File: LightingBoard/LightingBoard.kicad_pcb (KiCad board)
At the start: 2 copper layers, 51.7 x 46.2 mm, 58 parts, among them J1 Barrel_Jack_Switch, J2 LED Out, J3 LED Out, J4 Programming, J5 UART, U1 AP7384-50SA, U2 NCV833, U3 INA180A2, U4 LMR33630ADDA, U5 MCP4725xxx-xCH, U6 INA180A2, U7 LMR33630ADDA, U8 MCP4725xxx-xCH, U9 ATtiny2313A-S

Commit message: NO MORR DINOSAURR
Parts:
- removed U1: AP7384-50SA, Package_TO_SOT_SMD:SOT-23
- added U10: AP2120N-5.0TRG1, Package_TO_SOT_SMD:SOT-23, F.Cu at (117.1, 86.9)
- U9: value ATtiny2313A-S -> ATtiny841-SS; footprint Package_SO:SOIC-20W_7.5x12.8mm_P1.27mm -> Package_SO:SOIC-14_3.9x8.7mm_P1.27mm
- moved J5 22.7 mm to (110.0, 76.7), turned to 0 degrees
- moved J1 17.9 mm to (115.8, 65.9), turned to -90 degrees
- moved C2 17.9 mm to (119.9, 91.7), turned to -90 degrees
- moved C5 16.5 mm to (120.1, 86.9), turned to -90 degrees
- moved U9 14.9 mm to (117.3, 78.0), turned to 180 degrees
- moved R11 13.0 mm to (119.4, 83.8), turned to 0 degrees
- moved C4 10.1 mm to (114.0, 86.9), turned to -90 degrees
- moved C18 9.53 mm to (115.6, 83.8), turned to 0 degrees
- moved D1 8.44 mm to (114.8, 70.9)
- moved R21 7.77 mm to (118.1, 70.9)
- moved R20 3.18 mm to (121.2, 70.9), turned to -90 degrees
- moved C3 1.85 mm to (112.0, 93.0), turned to -90 degrees
- moved C1 1.61 mm to (111.5, 70.9), turned to -90 degrees
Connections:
- C18 pad 1: /Reset -> GND
- C18 pad 2: GND -> /Reset
- J4 pad 2: Net-(J4-Pin_2) -> /SCL
- J4 pad 3: /SDA -> /MISO(12)
- J4 pad 4: Net-(J4-Pin_4) -> /MOSI(11)
- J4 pad 5: /SCL -> /CS(10)
- R11 pad 1: +5V -> /Reset
- R11 pad 2: /Reset -> +5V
- R2 pad 2: /SDA -> /MOSI(11)
- R20 pad 1: /Reset -> /CS(10)
- R20 pad 2: Net-(J4-Pin_2) -> /Reset
- U5 pad 4: /SDA -> /MOSI(11)
- U8 pad 4: /SDA -> /MOSI(11)
- U9 pad 1: /Reset -> +5V
- U9 pad 10: GND -> /Enable1
- U9 pad 11: unconnected-(U9-PD6-Pad11) -> /UART_RX
- U9 pad 12: /PG2 -> /UART_TX
- U9 pad 13: /Enable2 -> /PG1
- U9 pad 14: /PG1 -> GND
- U9 pad 2: /UART_RX -> /PG2
- U9 pad 3: /UART_TX -> /Enable2
- U9 pad 4: GND -> /Reset
- U9 pad 5: GND -> /Status
- U9 pad 7: unconnected-(U9-PD3-Pad7) -> /MOSI(11)
- U9 pad 8: unconnected-(U9-PD4-Pad8) -> /MISO(12)
- U9 pad 9: unconnected-(U9-PD5-Pad9) -> /SCL
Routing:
- net /SDA: track 40.7 -> 0.00 mm, vias 3 -> 0
- net /MOSI(11): track 0.00 -> 21.7 mm, vias 0 -> 1
- net Net-(J4-Pin_4): track 21.7 -> 0.00 mm, vias 2 -> 0
- net /PG1: track 16.5 -> 32.5 mm, vias 0 -> 2
- net /Enable1: track 5.08 -> 19.2 mm, vias 0 -> 2
- net /Enable2: track 27.7 -> 14.3 mm
- net /PG2: track 38.1 -> 24.8 mm
- net /MISO(12): track 0.00 -> 12.3 mm
- net /Reset: track 26.0 -> 15.8 mm, vias 4 -> 3
- net GND: track 0.00 -> 9.36 mm, vias 32 -> 31
- net /SCL: track 39.0 -> 29.7 mm, vias 4 -> 3
- net +5V: track 62.5 -> 54.5 mm, vias 4 -> 3
- net Net-(J4-Pin_2): track 6.88 -> 0.00 mm
- net VCC: track 109.0 -> 102.2 mm, vias 7 -> 8
- net /CS(10): track 0.00 -> 5.59 mm
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
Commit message: HEHEHE
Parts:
- added C19: 100nF, Capacitor_SMD:C_0603_1608Metric, F.Cu at (134.4, 68.8)
- added C20: 10uF, Capacitor_SMD:C_0603_1608Metric, F.Cu at (132.3, 72.9)
- added C21: 100nF, Capacitor_SMD:C_0603_1608Metric, F.Cu at (134.4, 80.5)
- added C22: 10uF, Capacitor_SMD:C_0603_1608Metric, F.Cu at (132.3, 76.7)
- added C23: 1u, Capacitor_SMD:C_0603_1608Metric, F.Cu at (144.3, 76.5)
- added C24: 100nF, Capacitor_SMD:C_0603_1608Metric, F.Cu at (144.3, 73.2)
- C12, C6: value .1u -> 100nF
- C2: value 47u -> 10u
- R14, R5: value 4k -> 30k
- R18, R9: value 1k -> 10k
- U2: value NCV833 -> TL5580IDR
- moved C6 3.84 mm to (149.4, 72.6), turned to 0 degrees
- moved C12 3.84 mm to (149.4, 76.7), turned to 0 degrees
- moved R2 0.51 mm to (129.5, 76.7)
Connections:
- net /SCL renamed /SCL(13)
- C12 pad 1: VCC -> +5V
- C6 pad 1: VCC -> +5V
- U3 pad 5: VCC -> +5V
- U6 pad 5: VCC -> +5V
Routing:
- net +5V: track 54.5 -> 93.6 mm, vias 3 -> 6
- net VCC: track 102.2 -> 90.5 mm, vias 8 -> 5
- net Net-(U2B-+): track 5.10 -> 5.91 mm, vias 0 -> 2
- net /VDAC2: track 5.62 -> 6.31 mm
- net /MOSI(11): track 21.7 -> 21.1 mm
- net /Sum2: track 34.6 -> 33.9 mm
- net Net-(U2B--): track 8.20 -> 8.83 mm, vias 0 -> 2
- net GND: vias 31 -> 35

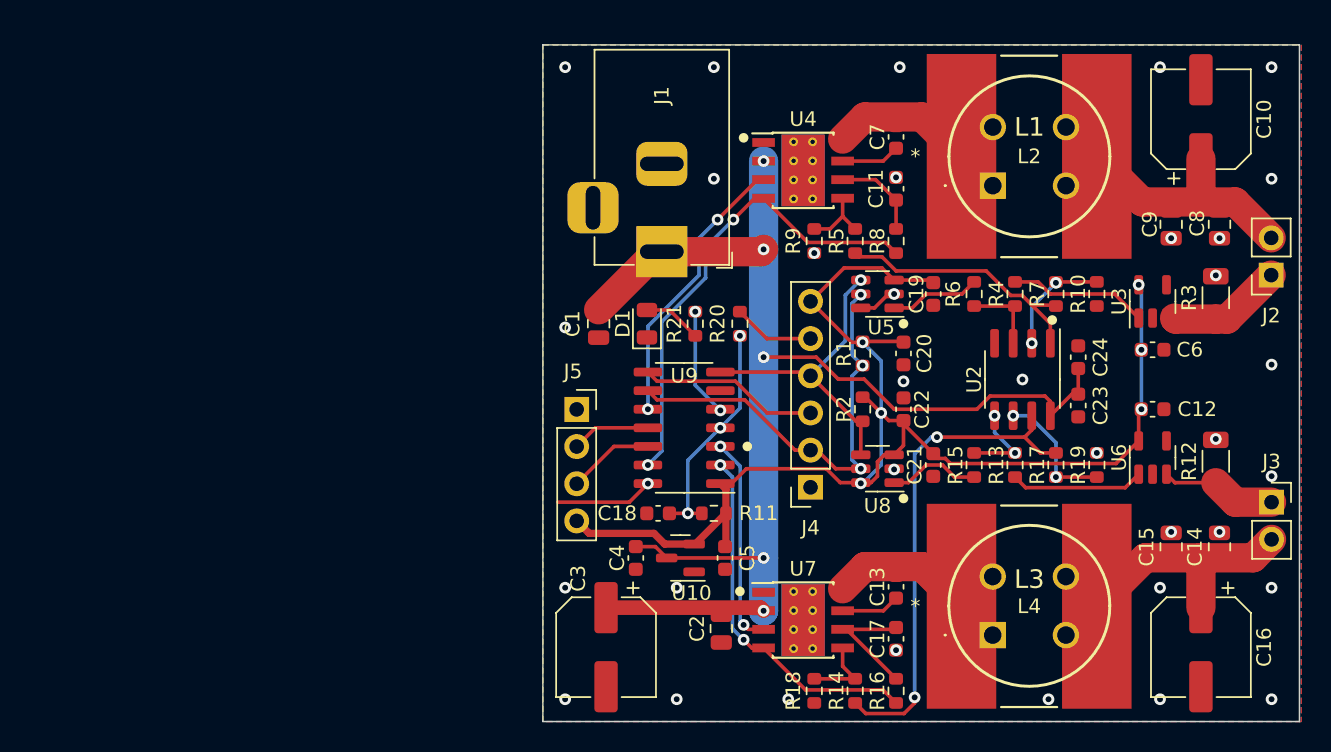
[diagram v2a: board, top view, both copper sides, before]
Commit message: new design based on AVR32DD20
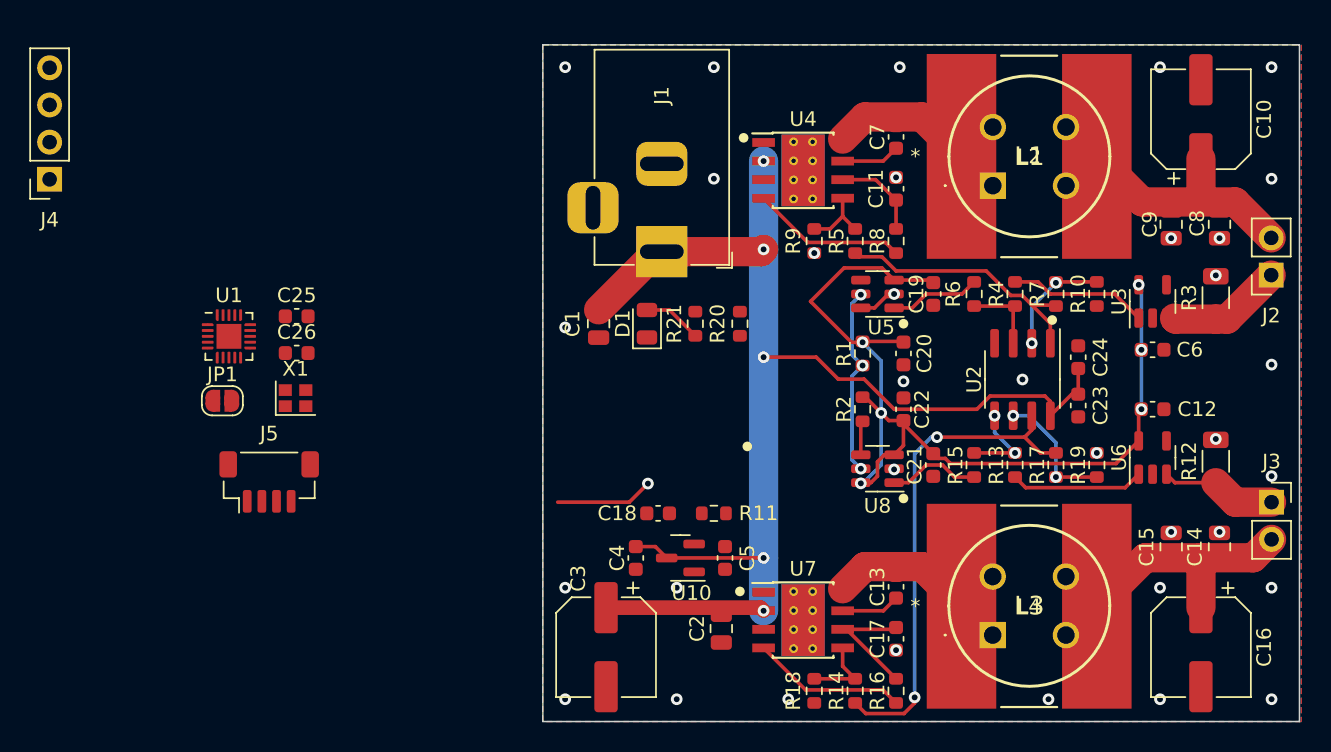
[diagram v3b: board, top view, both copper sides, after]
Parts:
- removed U9: ATtiny841-SS, Package_SO:SOIC-14_3.9x8.7mm_P1.27mm
- added C25: C_CLK, Capacitor_SMD:C_0603_1608Metric, F.Cu at (90.9, 70.4)
- added C26: C_CLK, Capacitor_SMD:C_0603_1608Metric, F.Cu at (90.9, 72.9)
- added JP1: SolderJumper_2_Open, Jumper:SolderJumper-2_P1.3mm_Open_RoundedPad1.0x1.5mm, F.Cu at (85.8, 76.1)
- added U1: AVR32DD20-E/REB, Package_DFN_QFN:VQFN-20-1EP_3x3mm_P0.4mm_EP1.7x1.7mm, F.Cu at (86.2, 71.7)
- added X1: XRCGB32M000F1S2KR0, Crystal:Crystal_SMD_2016-4Pin_2.0x1.6mm, F.Cu at (90.8, 76.0)
- J4: footprint Connector_PinSocket_2.54mm:PinSocket_1x06_P2.54mm_Vertical -> Connector_PinSocket_2.54mm:PinSocket_1x04_P2.54mm_Vertical
- J5: footprint Connector_PinSocket_2.54mm:PinSocket_1x04_P2.54mm_Vertical -> Connector_JST:JST_SH_BM04B-SRSS-TB_1x04-1MP_P1.00mm_Vertical
- L1, L3: footprint BuckParts:7447231101 -> CustomFootprints:7447231101
- L2, L4: footprint BuckParts:IND_BOURNS_SDR1307 -> CustomFootprints:IND_BOURNS_SDR1307
- R11: value 4.7k -> 330
- R20: value 330 -> 4.7K
- moved J4 56.1 mm to (74.0, 61.0)
- moved J5 21.6 mm to (89.0, 81.7)
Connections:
- C18 pad 2: /Reset -> Net-(U1-PF6(*RESET))
- J4 pad 2: /SCL(13) -> Net-(J4-Pin_2)
- J4 pad 3: /MISO(12) -> /Reset
- J4 pad 4: /MOSI(11) -> +5V
- J5 pad 2: /UART_RX -> +5V
- J5 pad 4: +5V -> /UART_RX
- R1 pad 2: /SCL(13) -> /SCL
- R11 pad 2: +5V -> Net-(U1-PF6(*RESET))
- R2 pad 2: /MOSI(11) -> /SDA
- R20 pad 1: /CS(10) -> /UPDI
- R20 pad 2: /Reset -> Net-(J4-Pin_2)
- U5 pad 4: /MOSI(11) -> /SDA
- U5 pad 5: /SCL(13) -> /SCL
- U8 pad 4: /MOSI(11) -> /SDA
- U8 pad 5: /SCL(13) -> /SCL
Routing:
- net /SCL(13): track 29.7 -> 0.00 mm, vias 3 -> 0
- net +5V: track 93.6 -> 66.7 mm
- net /PG1: track 32.5 -> 10.6 mm, vias 2 -> 0
- net /MOSI(11): track 21.1 -> 0.00 mm, vias 1 -> 0
- net /Enable1: track 19.2 -> 0.00 mm, vias 2 -> 0
- net /Reset: track 15.8 -> 0.00 mm, vias 3 -> 0
- net /Enable2: track 14.3 -> 0.00 mm, vias 2 -> 0
- net /PG2: track 24.8 -> 10.6 mm, vias 2 -> 0
- net /SCL: track 0.00 -> 13.0 mm, vias 0 -> 3
- net /MISO(12): track 12.3 -> 0.00 mm
- net /Status: track 7.46 -> 0.00 mm, vias 2 -> 0
- net /UART_TX: track 5.92 -> 0.00 mm
- net /CS(10): track 5.59 -> 0.00 mm
- net /UART_RX: track 5.40 -> 0.00 mm
- net /SDA: track 0.00 -> 1.97 mm

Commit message: update to kicad 8
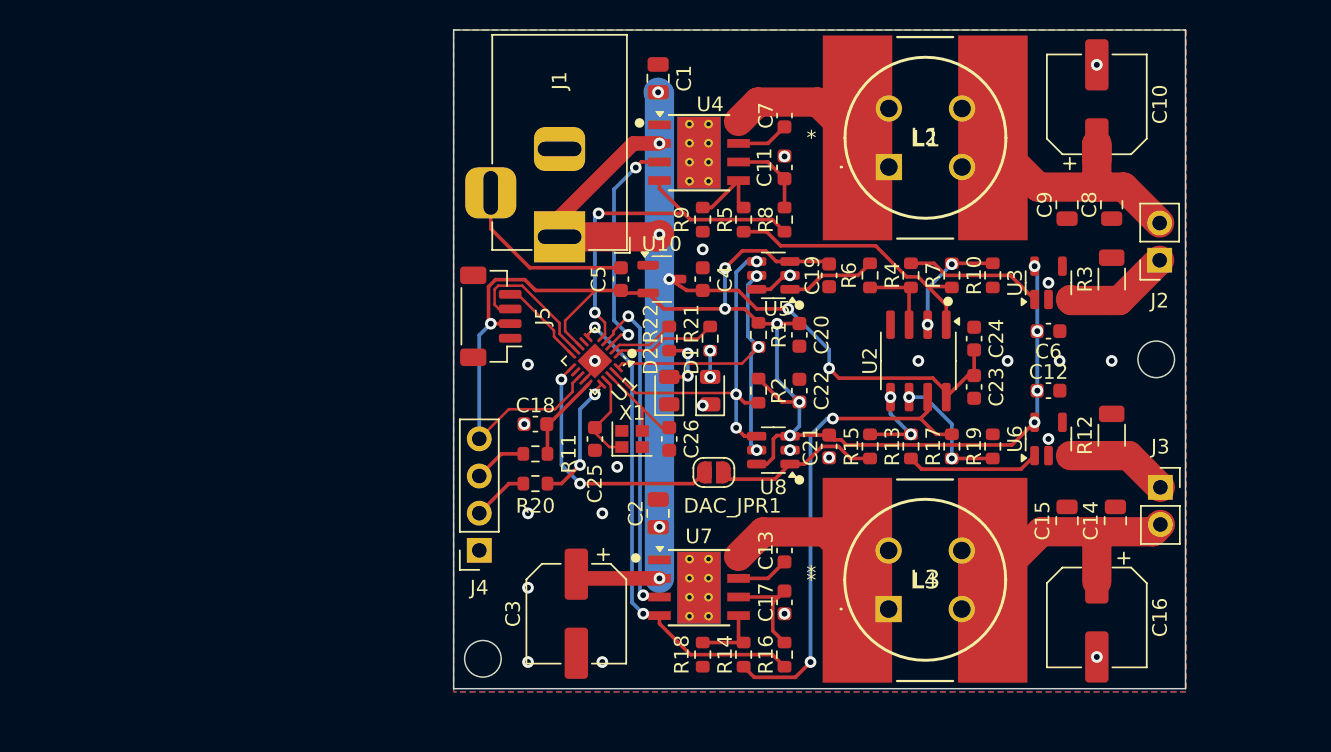
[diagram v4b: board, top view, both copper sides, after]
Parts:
- removed JP1: SolderJumper_2_Open, Jumper:SolderJumper-2_P1.3mm_Open_RoundedPad1.0x1.5mm
- added D2: LED, LED_SMD:LED_0805_2012Metric, F.Cu at (116.3, 75.4)
- added DAC_JPR1: SolderJumper_2_Open, Jumper:SolderJumper-2_P1.3mm_Open_RoundedPad1.0x1.5mm, F.Cu at (119.4, 81.0)
- added R22: 1K, Resistor_SMD:R_0603_1608Metric, F.Cu at (116.3, 71.9)
- U10: value AP2120N-5.0TRG1 -> XC6206P502MR
- moved J4 38.8 mm to (103.4, 86.3)
- moved C26 26.1 mm to (116.3, 78.7), turned to 90 degrees
- moved U1 25.1 mm to (111.3, 73.4), turned to -135 degrees
- moved X1 23.2 mm to (113.8, 78.7)
- moved C25 22.0 mm to (111.3, 78.7), turned to -90 degrees
- moved C5 20.3 mm to (113.0, 67.8), turned to 90 degrees
- moved C4 19.6 mm to (118.6, 67.8), turned to 90 degrees
- moved U10 19.1 mm to (115.8, 67.8), turned to 0 degrees
- moved J5 18.9 mm to (104.1, 70.4), turned to 90 degrees
- moved R20 17.7 mm to (107.2, 81.8), turned to 180 degrees
- moved C1 17.2 mm to (115.6, 54.1), turned to 90 degrees
- moved R11 12.9 mm to (107.2, 79.8)
- moved C18 10.4 mm to (107.2, 77.7)
- moved C2 8.98 mm to (115.6, 83.8), turned to 90 degrees
- moved C17 8.02 mm to (124.2, 89.9)
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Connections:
- net /Status renamed /Status1
- U1 pad 2: unconnected-(U1-PA5-Pad2) -> /Status2
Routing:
- net +5V: track 66.7 -> 105.7 mm, vias 6 -> 10
- net /Enable2: track 0.00 -> 23.0 mm, vias 0 -> 2
- net /SDA: track 1.97 -> 24.7 mm, vias 0 -> 3
- net /PG2: track 10.6 -> 33.3 mm, vias 0 -> 2
- net /AVR_DAC: track 0.00 -> 17.5 mm, vias 0 -> 2
- net /Enable1: track 0.00 -> 15.8 mm, vias 0 -> 2
- net /PG1: track 10.6 -> 25.4 mm, vias 0 -> 2
- net /UART_TX: track 0.00 -> 10.1 mm
- net /SCL: track 13.0 -> 23.0 mm
- net /UPDI: track 0.00 -> 8.88 mm, vias 0 -> 2
- net GND: track 9.36 -> 16.7 mm, vias 35 -> 24
- net /Status1: track 0.00 -> 7.07 mm
- net /XTAL2: track 0.00 -> 7.06 mm
- net /XTAL1: track 0.00 -> 6.43 mm
- net VCC: track 90.4 -> 84.0 mm, vias 5 -> 8
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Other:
- board size 51.7 x 46.2 mm -> 50 x 45 mm
